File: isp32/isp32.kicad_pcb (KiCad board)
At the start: 2 copper layers, 55.5 x 48.5 mm, 105 parts, among them J1 BAT1, J10 LoRa_ANT, J12 Micro_SD_Card, J2 Switching, J3 USB_C_Receptacle_USB2.0, J4 ESP_JTAG, J5 GPS_ANT, J6 F0, J7 F1, J9 ANT, M1 Motor_Servo, M2 Motor_Servo, M3 Motor_Servo, M4 Motor_Servo, Q1 BSS138, Q2 BSS138, Q3 IRLML6402, Q4 BSS138, Q5 IRLML6402, Q6 S8050, Q7 S8050, Q8 S8050, SW1 RST, SW2 IO0, U1 STM32G030J6M6, U10 BMP280, U11 MPU-9250, U12 CH340C, U2 USBLC6-2SC6, U3 ESP32-WROOM-32U, U4 AMS1117-3.3, U5 MP2303ADN, U6 24LC32, U7 NEO-XM, U9 RFM98W-315S2

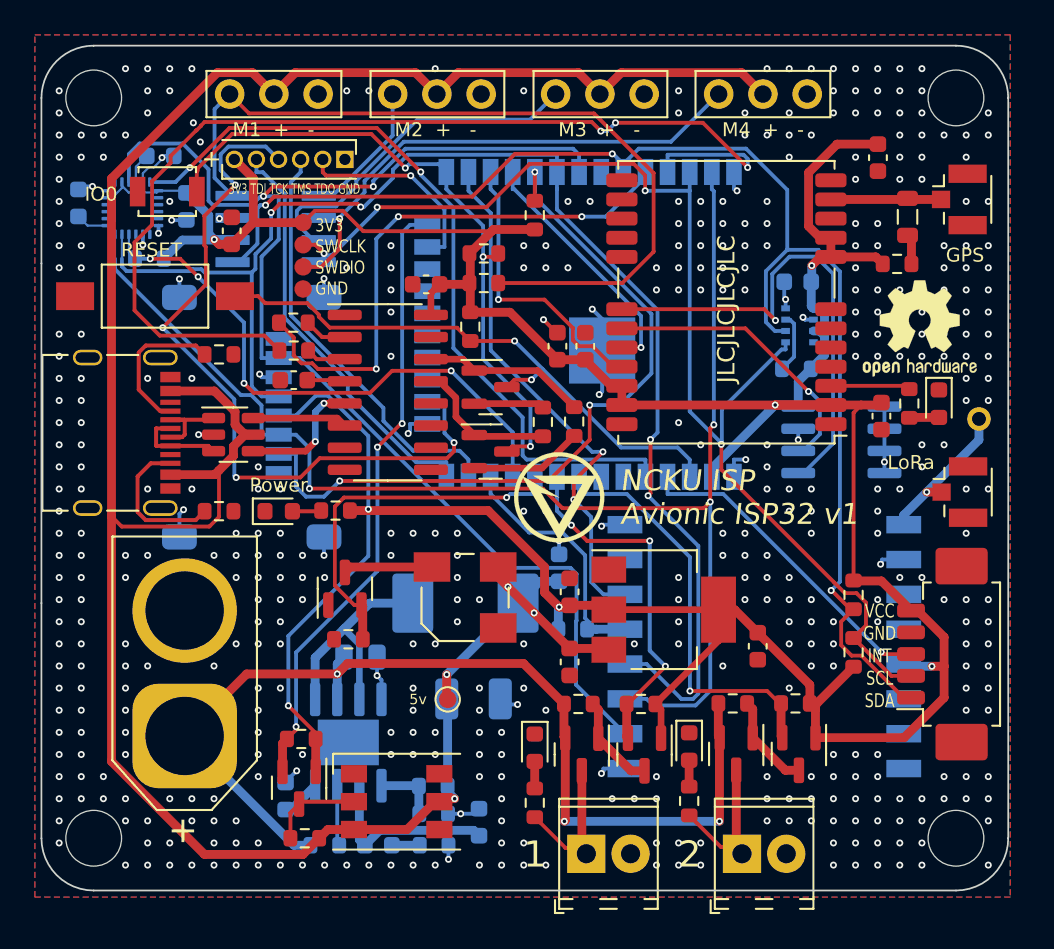
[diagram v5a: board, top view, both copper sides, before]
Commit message: New design with esp32s3
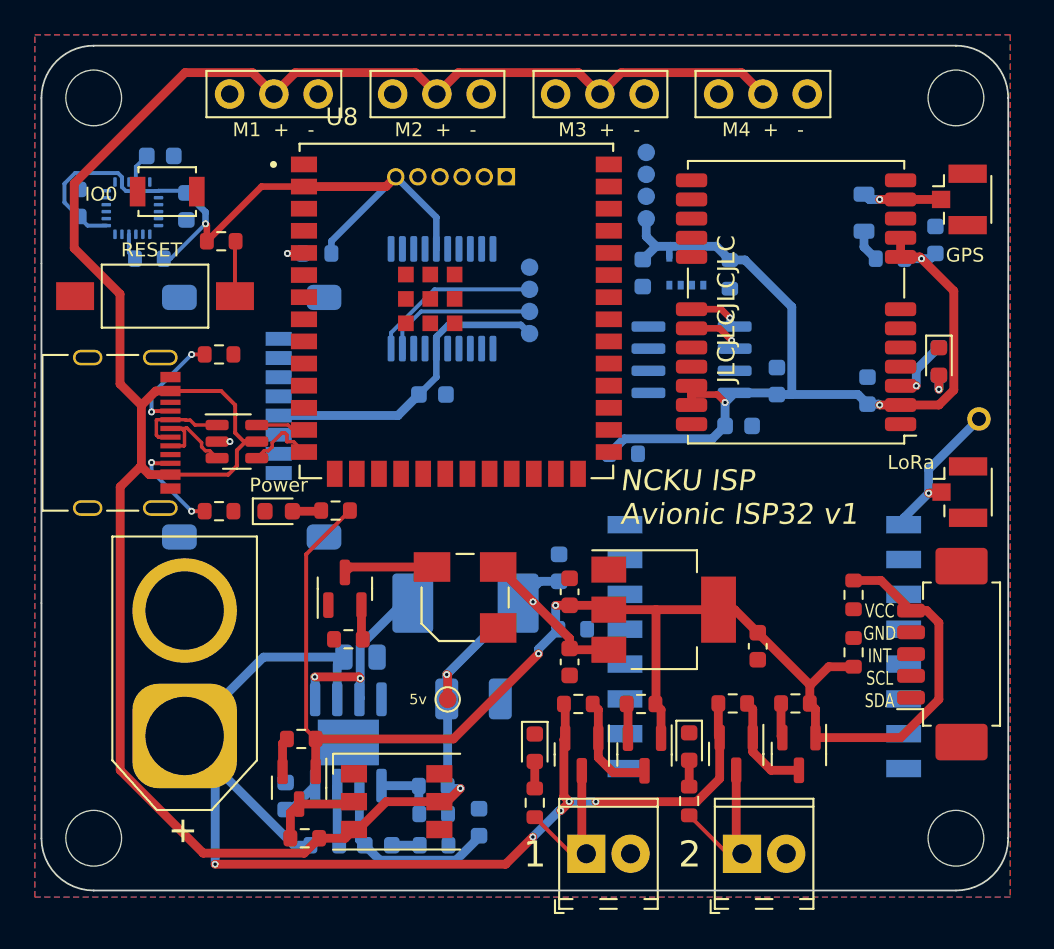
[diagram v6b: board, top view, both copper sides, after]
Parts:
- removed C25, C26: 100n, Capacitor_SMD:C_0603_1608Metric
- removed G***: LOGO, isp_logo:isp_logo
- removed Q7, Q8: S8050, Package_TO_SOT_SMD:SOT-23
- removed R26, R27: 470, Resistor_SMD:R_0603_1608Metric
- removed R28, R29, R3: 10k, Resistor_SMD:R_0603_1608Metric
- removed REF**: OSHW-Logo2_7.3x6mm_SilkScreen, Symbol:OSHW-Logo2_7.3x6mm_SilkScreen
- removed U1: STM32G030J6M6, STM32G030J6:SOIC127P600X175-8N
- removed U12: CH340C, Package_SO:SOIC-16_3.9x9.9mm_P1.27mm
- added TP6: 3V3, TestPoint:TestPoint_Pad_D1.0mm, B.Cu at (94.3, 47.7)
- added TP7: SWDIO, TestPoint:TestPoint_Pad_D1.0mm, B.Cu at (94.3, 46.4)
- added TP8: SWCLK, TestPoint:TestPoint_Pad_D1.0mm, B.Cu at (94.3, 45.2)
- added TP9: GND, TestPoint:TestPoint_Pad_D1.0mm, B.Cu at (94.3, 43.9)
- added U8: ESP32-S3-WROOM-1U, ESP32-S3-WROOM-1U:XCVR_ESP32-S3-WROOM-1U, F.Cu at (83.4, 53.0)
- C11, C13, C14, C3, C9, J4, L2, R12, R13, R2, R30, TP1, TP3, TP4, TP5: moved to B.Cu
- U3: value ESP32-WROOM-32U -> STM32F030F4Px; footprint RF_Module:ESP32-WROOM-32U -> Package_SO:TSSOP-20_4.4x6.5mm_P0.65mm
- moved R1 15.1 mm to (69.9, 49.0), turned to 0 degrees
- moved C3 14.9 mm to (82.0, 57.8), turned to 0 degrees
- moved TP1 14.5 mm to (87.6, 54.3)
- moved R2 14.0 mm to (93.0, 61.2)
- moved TP3 13.2 mm to (87.6, 53.0), turned to 90 degrees
- moved TP4 13.2 mm to (87.6, 51.8), turned to 90 degrees
- moved TP5 13.1 mm to (87.6, 50.5), turned to 90 degrees
- moved C13 12.8 mm to (101.8, 57.0)
- moved R30 12.7 mm to (75.4, 49.7), turned to 180 degrees
- moved C11 9.92 mm to (99.6, 59.6), turned to 0 degrees
- moved U6 9.75 mm to (96.9, 55.8), turned to 0 degrees
- moved J4 9.32 mm to (86.3, 45.3), turned to 90 degrees
- moved C16 8.91 mm to (94.1, 50.8), turned to -90 degrees
- moved U3 8.63 mm to (82.6, 52.3), turned to -90 degrees
- moved U10 7.20 mm to (96.6, 50.7), turned to 0 degrees
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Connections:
- net Net-(J3-PadA6) renamed UD+
- net Net-(J3-PadA7) renamed UD-
- TP3 pad 1: SERVO3 -> SWDIO
- TP4 pad 1: SCL -> SWCLK
- U3 pad 10: Buzz -> unconnected-(U3-Pad10)
- U3 pad 11: IMU_SS -> unconnected-(U3-Pad11)
- U3 pad 12: LORA_SS -> unconnected-(U3-Pad12)
- U3 pad 13: TMS -> unconnected-(U3-Pad13)
- U3 pad 14: TDI -> unconnected-(U3-Pad14)
- U3 pad 16: TCK -> +3V3
- U3 pad 17: unconnected-(U3-Pad17) -> SCL
- U3 pad 18: unconnected-(U3-Pad18) -> SDA
- U3 pad 19: unconnected-(U3-Pad19) -> SWDIO
- U3 pad 2: +3V3 -> unconnected-(U3-Pad2)
- U3 pad 20: unconnected-(U3-Pad20) -> SWCLK
- U3 pad 3: RST -> unconnected-(U3-Pad3)
- U3 pad 4: EXT_INT -> RST
- U3 pad 5: IMU_INT -> +3V3
- U3 pad 6: unconnected-(U3-Pad6) -> SERVO0
- U3 pad 7: unconnected-(U3-Pad7) -> SERVO1
- U3 pad 8: FIRE0 -> SERVO2
- U3 pad 9: FIRE1 -> SERVO3
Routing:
- net SCK: track 79.9 -> 0.00 mm, vias 4 -> 0
- net MOSI: track 79.7 -> 0.00 mm, vias 3 -> 0
- net SDA: track 78.6 -> 0.00 mm, vias 3 -> 0
- net MISO: track 77.0 -> 0.00 mm, vias 2 -> 0
- net SCL: track 69.7 -> 0.00 mm, vias 4 -> 0
- net RXD: track 60.6 -> 0.00 mm, vias 3 -> 0
- net SERVO0: track 47.0 -> 0.00 mm
- net IMU_INT: track 44.7 -> 0.00 mm, vias 2 -> 0
- net GND: track 44.3 -> 0.00 mm, vias 461 -> 1
- net TCK: track 43.4 -> 0.00 mm, vias 4 -> 0
- net SD_SS: track 43.6 -> 1.84 mm, vias 3 -> 1
- net IO0: track 37.7 -> 0.00 mm, vias 3 -> 0
- net RGB: track 35.4 -> 1.97 mm, vias 3 -> 0
- net TXD: track 32.0 -> 0.00 mm, vias 3 -> 0
- net IMU_SS: track 33.0 -> 1.54 mm, vias 4 -> 0
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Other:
- board text added: "3V3 SWDIO SWCLK GND"
- board text removed: "3V3 SWCLK SWDIO GND"

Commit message: Complete routing
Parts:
- added G***: LOGO, isp_logo:isp_logo, B.Cu at (87.0, 61.1)
- added REF**: OSHW-Logo2_7.3x6mm_SilkScreen, Symbol:OSHW-Logo2_7.3x6mm_SilkScreen, F.Cu at (107.8, 79.1)
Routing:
- net MISO: track 0.00 -> 65.5 mm, vias 0 -> 2
- net TX1: track 0.00 -> 63.8 mm
- net SDA: track 0.00 -> 59.0 mm, vias 0 -> 2
- net MOSI: track 0.00 -> 57.9 mm, vias 0 -> 1
- net SCL: track 0.00 -> 55.6 mm, vias 0 -> 3
- net RX1: track 0.00 -> 54.7 mm
- net SCK: track 0.00 -> 53.9 mm, vias 0 -> 2
- net IO0: track 0.00 -> 46.8 mm, vias 0 -> 1
- net EXT_INT: track 0.00 -> 44.9 mm, vias 0 -> 2
- net GND: track 0.00 -> 43.5 mm, vias 1 -> 485
- net SERVO1: track 0.00 -> 42.6 mm
- net +3V3: track 199.8 -> 242.0 mm, vias 6 -> 9
- net SD_SS: track 1.84 -> 43.8 mm
- net Buzz: track 1.99 -> 38.0 mm, vias 0 -> 2
- net LORA_SS: track 0.00 -> 34.5 mm, vias 0 -> 1
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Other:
- board text added: "GND RXD TXD 3V3"
- board text added: "GND SWCLK SWDIO 3V3"
- board text added: "GND TDO TMS TCK TDI 3V3"
- board text removed: "3V3 SWDIO SWCLK GND"
- board text removed: "3V3 TDI TCK TMS TDO GND"

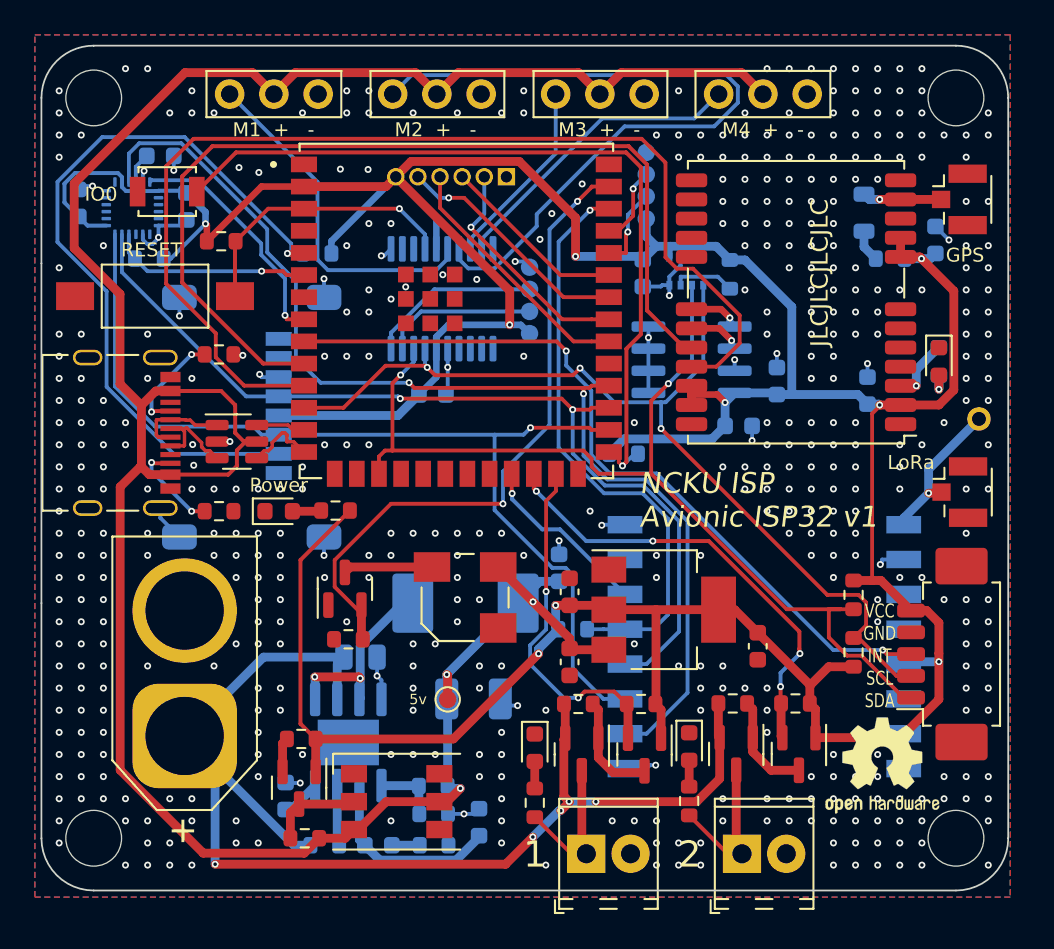
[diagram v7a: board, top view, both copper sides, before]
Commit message: Change power circuits
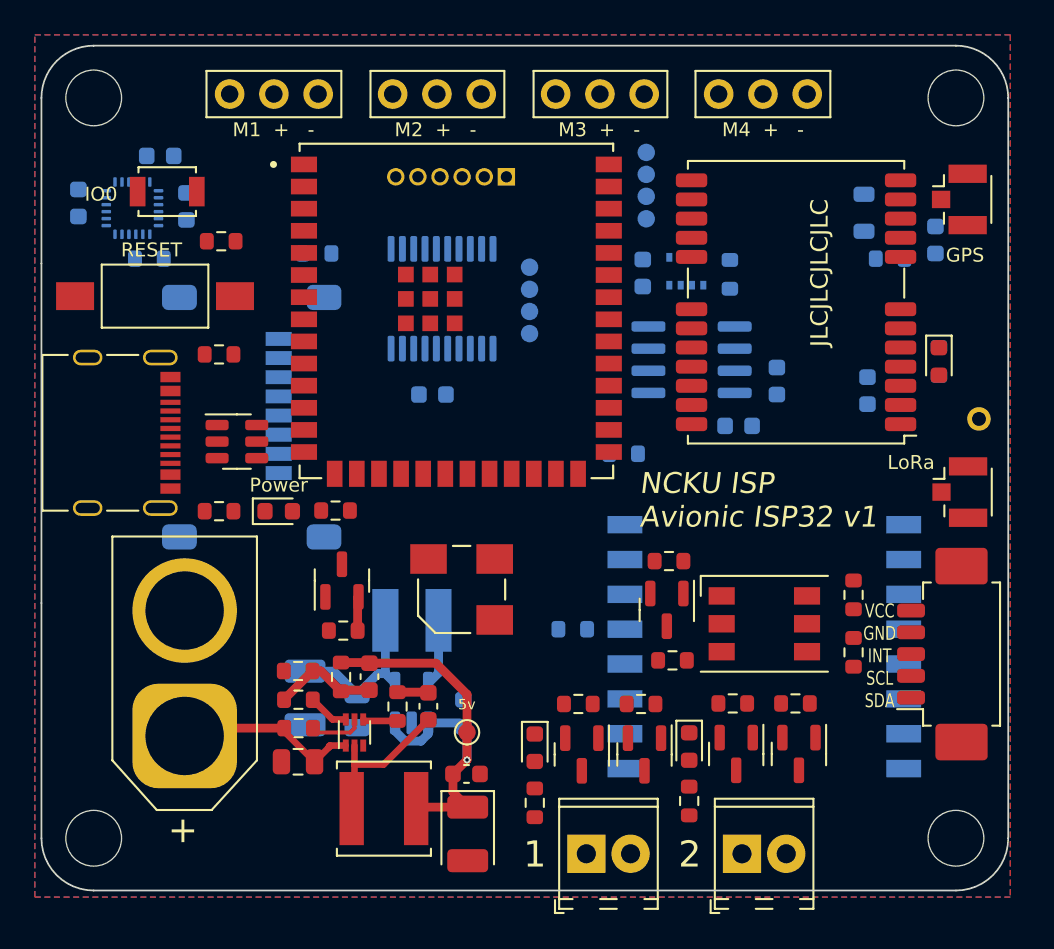
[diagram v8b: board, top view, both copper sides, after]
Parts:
- removed C12: 2.2n, Capacitor_SMD:C_0603_1608Metric
- removed C15: 47u, Capacitor_SMD:C_0603_1608Metric
- removed REF**: OSHW-Logo2_7.3x6mm_SilkScreen, Symbol:OSHW-Logo2_7.3x6mm_SilkScreen
- removed U5: MP2303ADN, Package_SO:SOIC-8-1EP_3.9x4.9mm_P1.27mm_EP2.62x3.51mm
- added C7: 10p, Capacitor_SMD:C_0603_1608Metric, F.Cu at (78.4, 74.0)
- added L3: 4.7u, Inductor_SMD:L_Sunlord_SWPA5020S, F.Cu at (79.2, 81.6)
- added R3: 100k, Resistor_SMD:R_0603_1608Metric, F.Cu at (74.3, 77.0)
- added U1: SC189ZSKTRT, Package_TO_SOT_SMD:SOT-23-5, B.Cu at (80.8, 75.5)
- C1: value 100n -> 22u; moved to B.Cu
- C10: value 50p -> 220u; footprint Capacitor_SMD:C_0603_1608Metric -> Capacitor_Tantalum_SMD:CP_EIA-3528-12_Kemet-T
- C2, C5: moved to F.Cu
- C6: value 1u -> 22u; footprint Capacitor_SMD:C_0603_1608Metric -> Capacitor_SMD:C_0805_2012Metric; moved to B.Cu
- C8: value 100n -> 22u; moved to F.Cu
- L1: value 10u -> 1u; footprint Inductor_SMD:L_Abracon_ASPI-0630LR -> Inductor_SMD:L_Bourns-SRN4018
- R10: value 10k -> 5.49k; moved to F.Cu
- R11: value 52.5k -> 40.2k; moved to F.Cu
- R8: value 100k -> 10; moved to F.Cu
- R9: value 91k -> 18k; moved to F.Cu
- U4: value AMS1117-3.3 -> MP1660GTF-Z; footprint Package_TO_SOT_SMD:SOT-223-3_TabPin2 -> Package_TO_SOT_SMD:SOT-563
- moved D3 23.4 mm to (101.1, 71.0)
- moved Q2 23.4 mm to (95.5, 70.2)
- moved R19 23.4 mm to (95.6, 67.4)
- moved R21 23.4 mm to (95.8, 73.1)
- moved C6 23.3 mm to (77.7, 76.0)
- moved U4 19.1 mm to (77.5, 77.2), turned to 90 degrees
- moved C10 12.3 mm to (74.7, 75.2), turned to -90 degrees
- moved R9 11.4 mm to (74.3, 75.3), turned to 180 degrees
- moved R10 11.3 mm to (74.3, 73.7), turned to 180 degrees
- moved C8 10.5 mm to (84.0, 79.6), turned to 0 degrees
- moved C4 10.4 mm to (81.8, 75.7), turned to -90 degrees
- moved R8 8.99 mm to (80.0, 75.7), turned to 90 degrees
- moved R11 8.20 mm to (76.8, 74.0), turned to 90 degrees
- moved C2 7.76 mm to (84.0, 83.0), turned to -90 degrees
- moved C5 7.00 mm to (74.3, 78.9), turned to 180 degrees
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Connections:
- C10 pad 1: Net-(C10-Pad1) -> +3V3
- C4 pad 1: +3V3 -> Net-(C4-Pad1)
- C4 pad 2: GND -> Net-(C4-Pad2)
- C8 pad 1: Net-(C8-Pad1) -> +5V
- L1 pad 2: +5V -> +3V3
- R10 pad 1: Net-(R10-Pad1) -> Net-(C7-Pad1)
- R11 pad 1: Net-(R10-Pad1) -> Net-(C7-Pad1)
- R8 pad 1: +BATT -> Net-(R8-Pad1)
- R8 pad 2: Net-(R8-Pad2) -> Net-(C4-Pad1)
- R9 pad 1: Net-(C12-Pad2) -> Net-(R9-Pad1)
- R9 pad 2: GND -> Net-(C7-Pad1)
- U4 pad 1: GND -> +BATT
- U4 pad 2: +3V3 -> Net-(C4-Pad2)
- U4 pad 3: +5V -> GND
- U8 pad 31: unconnected-(U8-Pad31) -> LORA_INT
- U9 pad 14: unconnected-(U9-Pad14) -> LORA_INT
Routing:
- net +3V3: track 242.0 -> 9.51 mm, vias 9 -> 0
- net +5V: track 148.4 -> 25.5 mm, vias 3 -> 1
- net MISO: track 65.5 -> 0.00 mm, vias 2 -> 0
- net TX1: track 63.8 -> 0.00 mm
- net +BATT: track 72.7 -> 10.8 mm, vias 5 -> 0
- net SDA: track 59.0 -> 0.00 mm, vias 2 -> 0
- net MOSI: track 57.9 -> 0.00 mm, vias 1 -> 0
- net SCL: track 55.6 -> 0.00 mm, vias 3 -> 0
- net RX1: track 54.7 -> 0.00 mm
- net SCK: track 53.9 -> 0.00 mm, vias 2 -> 0
- net IO0: track 46.8 -> 0.00 mm, vias 1 -> 0
- net EXT_INT: track 44.9 -> 0.00 mm, vias 2 -> 0
- net SD_SS: track 43.8 -> 0.00 mm, vias 1 -> 0
- net GND: track 43.5 -> 0.00 mm, vias 485 -> 0
- net SERVO1: track 42.6 -> 0.00 mm
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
